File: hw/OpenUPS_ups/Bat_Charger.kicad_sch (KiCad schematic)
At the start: 68 parts, among them Q601 2N7002, Q701 Q_NMOS_GDS, Q702 Q_NMOS_GDS, Q901 PMOS, U402 BD99950, U502 INA181A1, U503 MCP6001R, U504 MCP6001R, U801 NCP431, U901 DZDH0401DW

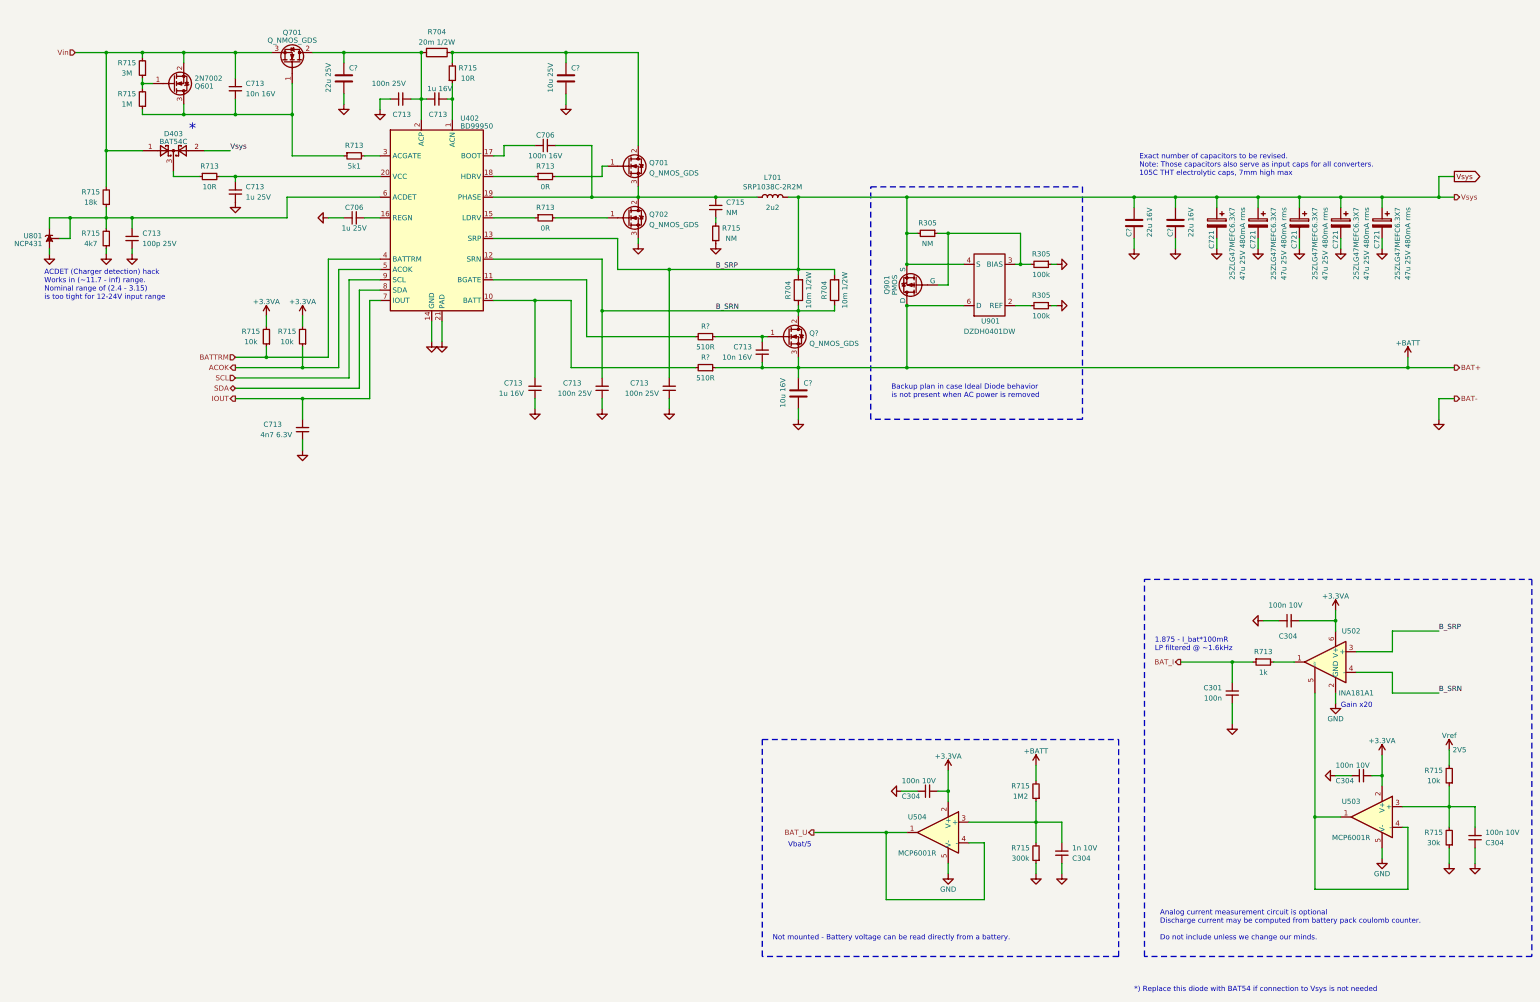
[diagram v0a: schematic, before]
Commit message: Preliminary NMOS: AON7534; USB-C selected.
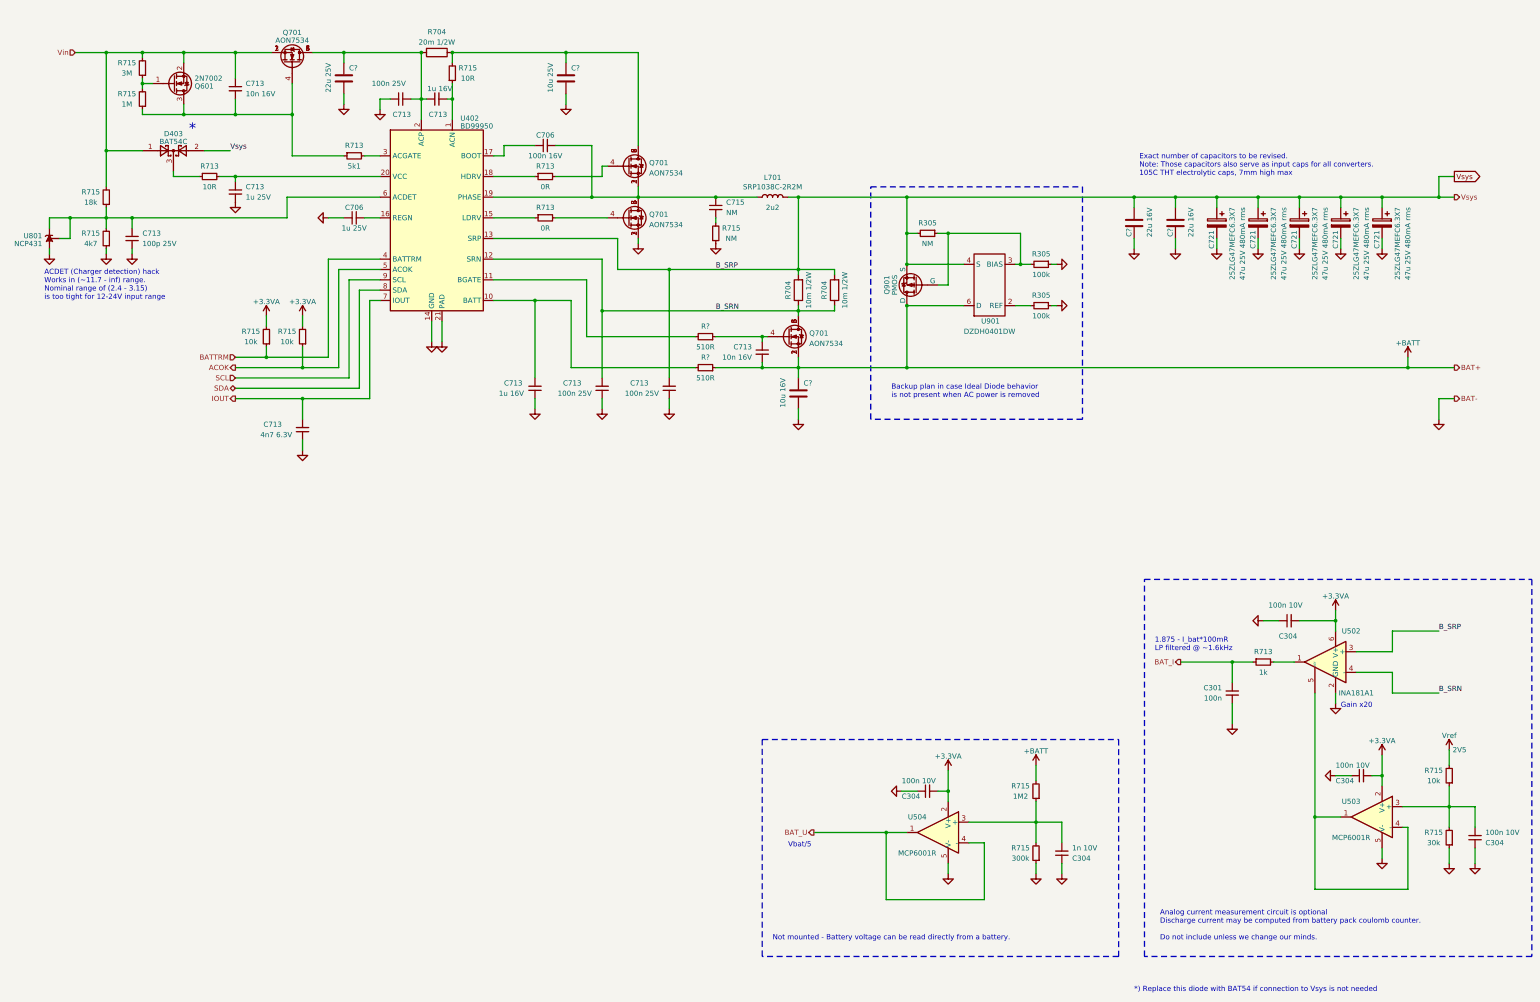
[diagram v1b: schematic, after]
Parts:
- removed Q701, Q702, Q?: Q_NMOS_GDS, Package_TO_SOT_SMD:TO-263-2, symbol Device:Q_NMOS_GDS
- added Q701 (x3): AON7534, footprints:DFN 3x3 MOSFET, symbol Device:Q_NMOS_GDS
- Q701: value Q_NMOS_GDS -> AON7534; footprint Package_TO_SOT_SMD:TO-263-2 -> footprints:DFN 3x3 MOSFET
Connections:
- net +BATT: now also Q701.1 (S), Q701.2 (S), Q701.3 (S)
- net B_SRN: now also Q701.5 (D), Q701.6 (D), Q701.7 (D), Q701.8 (D)
- net GND: now also Q701.1 (S), Q701.2 (S), Q701.3 (S)
- net Vin: now also Q701.1 (S), Q701.2 (S), Q701.3 (S)
- net at R713.2: now also Q701.4 (G)
- net at C?.1, R704.1, R715.2: now also Q701.5 (D), Q701.6 (D), Q701.7 (D), Q701.8 (D); no longer Q701.2 (D)
- net at C713.2, Q601.3 (D), R713.1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: now also Q701.4 (G)
- net at C713.1, R?.1: now also Q701.4 (G)
- net at C713.1, C713.2, C?.1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: now also Q701.5 (D), Q701.6 (D), Q701.7 (D), Q701.8 (D)
- net at R713.2: now also Q701.4 (G); no longer Q701.1 (G)
- net at C706.2, C715.1, L701.1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: now also Q701.1 (S), Q701.2 (S), Q701.5 (D), Q701.6 (D), Q701.7 (D), Q701.8 (D)

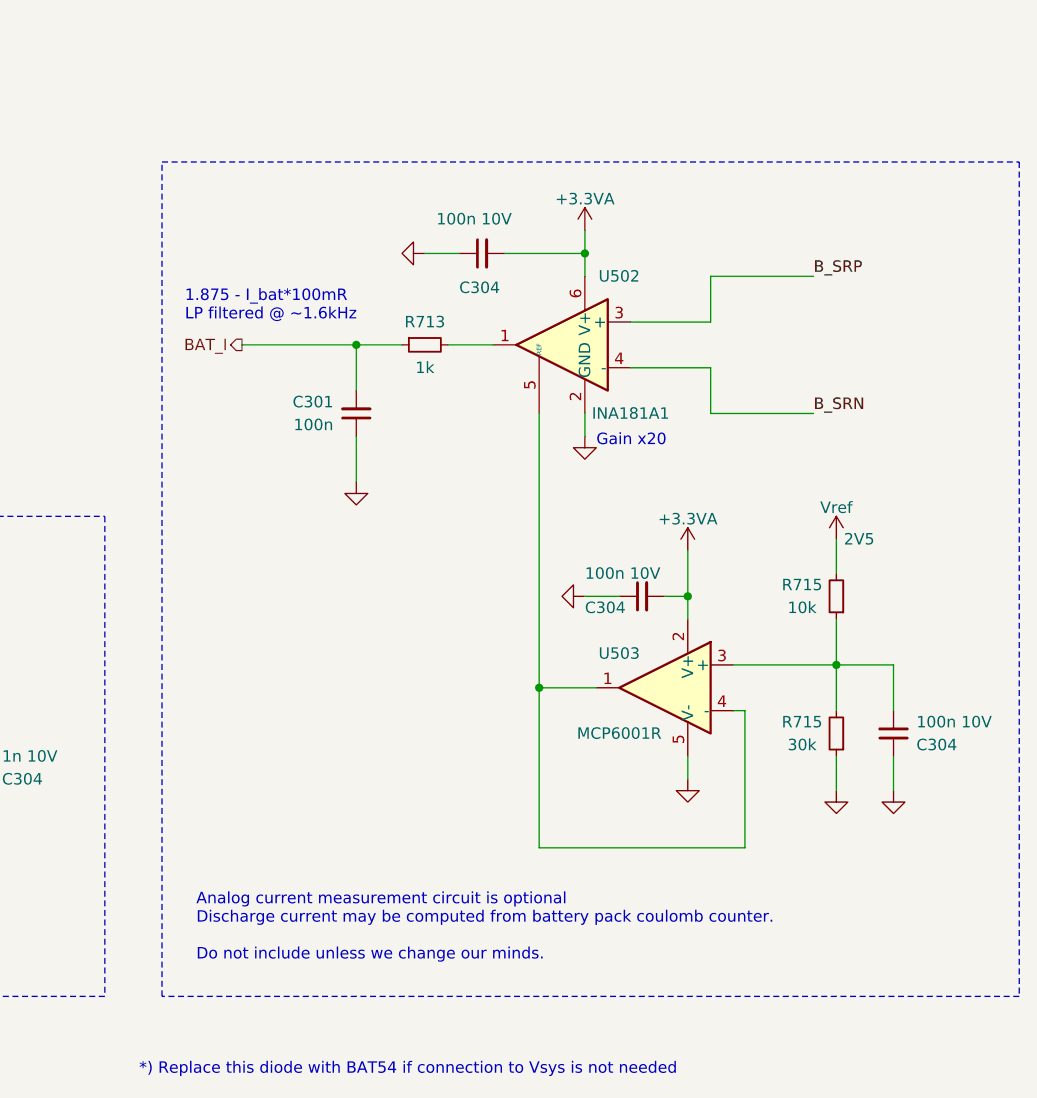
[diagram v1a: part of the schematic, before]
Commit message: Removed Vref (AVR has its own). Replaced INA181s with INA180s
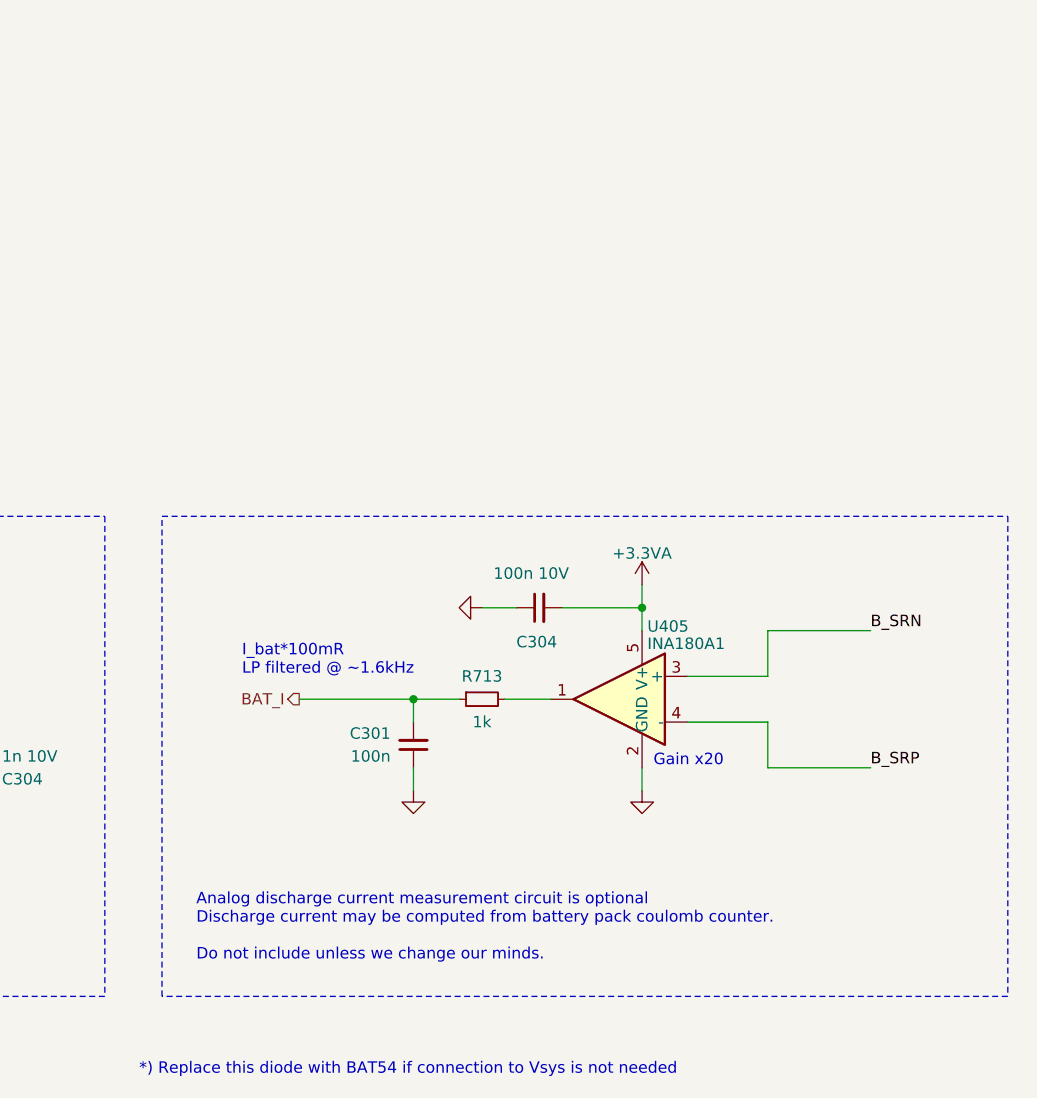
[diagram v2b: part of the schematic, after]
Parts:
- removed C304 (x2): 100n 10V, Capacitor_SMD:C_0603_1608Metric, symbol Device:C_Small
- removed R715: 30k, Resistor_SMD:R_0603_1608Metric, symbol Device:R_Small
- removed R715: 10k, Resistor_SMD:R_0603_1608Metric, symbol Device:R_Small
- removed U502: INA181A1, Package_TO_SOT_SMD:SOT-23-6, symbol Amplifier_Current:INA181
- removed U503: MCP6001R, Package_TO_SOT_SMD:SOT-23-5, symbol Amplifier_Operational:MCP6001R
- added U405: INA180A1, Package_TO_SOT_SMD:SOT-23-5, symbol Amplifier_Current:INA180A1
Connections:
- net +3.3VA: now also U405.5 (V+)
- net B_SRN: now also U405.3 (+)
- net GND: now also U405.2 (GND)
- net Vsys: now also U405.4 (-)
- net at R713.2: now also U405.1
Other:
- note added: "Analog discharge current measurement circuit is optional Discharge current may be computed from battery pack coulomb counter. Do not include unless we change our minds."
- note added: "I_bat*100mR LP filtered @ ~1.6kHz"
- note removed: "1.875 - I_bat*100mR LP filtered @ ~1.6kHz"
- note removed: "Analog current measurement circuit is optional Discharge current may be computed from battery pack coulomb counter. Do not include unless we change our minds."
- moved on the sheet: C301, C304, R713

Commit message: Initial placement effort
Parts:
- renumbered D403 to D401, U504 to U403

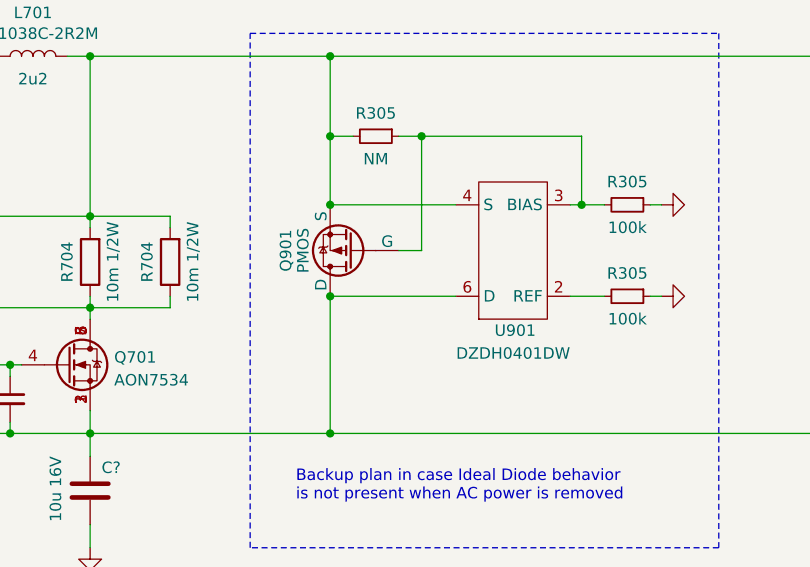
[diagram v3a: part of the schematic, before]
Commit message: Layout: Component models, mechanical, connectors
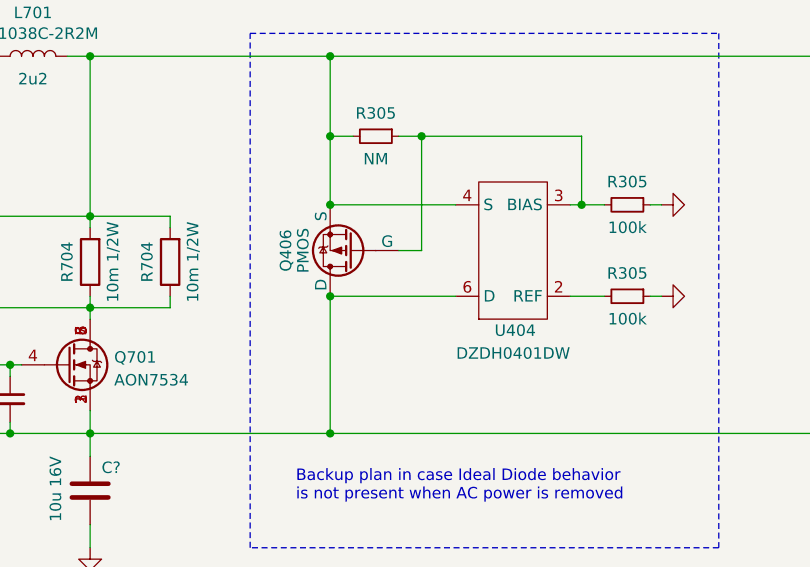
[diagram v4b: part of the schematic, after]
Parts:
- renumbered Q901 to Q406, U901 to U404
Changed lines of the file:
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@@
   (symbol (lib_id "Simulation_SPICE:PMOS") (at 247.65 82.55 180) (unit 1)
     (in_bom yes) (on_board yes) (dnp no) (fields_autoplaced)
-    (property "Reference" "Q901" (at 240.1951 82.55 90)
+    (property "Reference" "Q406" (at 240.1951 82.55 90)
       (effects (font (size 1.27 1.27)))
     )
@@
   (symbol (lib_id "OpenUPS_ups:DZDH0401DW") (at 261.62 82.55 90) (unit 1)
     (in_bom yes) (on_board yes) (dnp no)
-    (property "Reference" "U901" (at 267.97 91.44 90)
-      (effects (font (size 1.27 1.27)) (justify left))
-    )
+    (property "Reference" "U404" (at 267.97 91.44 90)
+      (effects (font (size 1.27 1.27)) (justify left))
+    )
